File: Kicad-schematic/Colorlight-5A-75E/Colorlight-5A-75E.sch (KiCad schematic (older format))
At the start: 97 parts, among them J1 HUB75 port, J10 HUB75 port, J11 HUB75 port, J12 HUB75 port, J13 HUB75 port, J14 HUB75 port, J15 HUB75 port, J16 HUB75 port, J19 Connector, J2 HUB75 port, J27 JTAG: TCK, J28 SW_Push, J3 HUB75 port, J30 JTAG: TDO, J31 JTAG: TMS, J32 JTAG: TDI, J33 3.3V, J34 GND, J4 HUB75 port, J5 HUB75 port, J6 HUB75 port, J7 HUB75 port, J8 HUB75 port, J9 HUB75 port, U10 74HC245, U11 74HC245, U12 74HC245, U13 74HC245, U14 74HC245, U15 74HC245, U16 74HC245, U17 74HC245, U18 74HC245, U19 74HC245, U20 74HC245, U21 74HC245, U22 74HC245, U23 74HC245, U24 74HC245, U25 74HC245, U26 74HC245, U27 74HC245, U28 74HC245, U29 M12L16161A, U30 74HC245, U31 W25Q32JVSSIQ, U32 M12L16161A, U33 LFE5U-25F-6BG256C, U38 74HC245, U39 74HC245, U9 74HC245

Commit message: Revert "Add nomenclature connections"
This reverts commit 12718895a0fb5e613c60318a09c710380de19625.
Fix issues
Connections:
- net labels added: +3.3V, GND, J1_1, J1_2, J1_3, J1_5, J1_6, J1_7, Jx_B16, Jx_F12, Jx_F15, Jx_J14, Jx_J5, Jx_K1, Jx_K2, Jx_L2, PL2B, PL2C, PT11B, PT15B, PT18A, PT18B, PT22A, PT22B, PT24A, PT24B, PT27A, PT27B, PT29A, PT33A, PT35A, PT38A, PT38B, PT40A, PT40B, PT42A, PT44B, PT47A, PT47B, PT49B, PT4A, PT4B, PT51A, PT53A, PT56A, PT56B, PT60A, PT62A, SPI_CCLK, SPI_CS, SPI_MISO, SPI_MOSI, TCK, TDI, TDO, TMS, U32_A4, U32_A7, U32_A8, U32_A9, U32_B10, U32_B11, U32_B12, U32_B7, U32_B8, U32_C12, U32_C4, U32_C6, U32_C7, U32_C8, U32_D10, U32_D11, U32_D13, U32_D3, U32_D4, U32_D5, U32_D6, U32_D7, U32_D8, U32_D9, U32_E10, U32_E11, U32_E2, U32_E4, U32_E5, U32_E6, U32_E7, U32_E9
- wire segments 256 -> 544
- no-connect marks 0 -> 1
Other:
- moved on the sheet: U29, U33

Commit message: Add nomenclature connections
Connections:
- net labels removed: +3.3V, GND, J1_1, J1_2, J1_3, J1_5, J1_6, J1_7, Jx_B16, Jx_F12, Jx_F15, Jx_J14, Jx_J5, Jx_K1, Jx_K2, Jx_L2, PL2B, PL2C, PT11B, PT15B, PT18A, PT18B, PT22A, PT22B, PT24A, PT24B, PT27A, PT27B, PT29A, PT33A, PT35A, PT38A, PT38B, PT40A, PT40B, PT42A, PT44B, PT47A, PT47B, PT49B, PT4A, PT4B, PT51A, PT53A, PT56A, PT56B, PT60A, PT62A, SPI_CCLK, SPI_CS, SPI_MISO, SPI_MOSI, TCK, TDI, TDO, TMS, U32_A4, U32_A7, U32_A8, U32_A9, U32_B10, U32_B11, U32_B12, U32_B7, U32_B8, U32_C12, U32_C4, U32_C6, U32_C7, U32_C8, U32_D10, U32_D11, U32_D13, U32_D3, U32_D4, U32_D5, U32_D6, U32_D7, U32_D8, U32_D9, U32_E10, U32_E11, U32_E2, U32_E4, U32_E5, U32_E6, U32_E7, U32_E9
- wire segments 544 -> 256
- no-connect marks 1 -> 0
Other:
- moved on the sheet: U29, U33

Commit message: Add Memory Connections
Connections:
- net labels added: +3.3V, GND, PL2B, PL2C, PT11B, PT15B, PT18A, PT18B, PT22A, PT22B, PT24A, PT24B, PT27A, PT27B, PT29A, PT33A, PT35A, PT38A, PT38B, PT40A, PT40B, PT42A, PT44B, PT47A, PT47B, PT49B, PT4A, PT4B, PT51A, PT53A, PT56A, PT56B, PT60A, PT62A, SPI_CCLK, SPI_CS, SPI_MISO, SPI_MOSI, TCK, TDI, TDO, TMS
- wire segments 256 -> 116
- no-connect marks 0 -> 1
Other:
- moved on the sheet: U29, U33

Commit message: Add U32 connection
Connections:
- net +3V3: now also U32.34 (CKE)
- net GND: now also J1.4 (Pin_4), U32.14 (LDQM), U32.18 (~CS), U32.36 (UDQM)
- net PT22A: now also U32.35 (CLK)
- net PT24A: now also U32.16 (~CAS)
- net PT24B: now also U32.17 (~RAS)
- net PT27A: now also U32.15 (~WE)
- net PT27B: now also U32.32 (A9)
- net PT29A: now also U32.19 (BA)
- net PT35A: now also U32.20 (A10/AP)
- net PT40A: now also U32.31 (A8)
- net PT40B: now also U32.30 (A7)
- net PT42A: now also U32.21 (A0)
- net PT47A: now also U32.29 (A6)
- net PT51A: now also U32.28 (A5)
- net PT56A: now also U32.23 (A2)
- net PT56B: now also U32.27 (A4)
- net PT62A: now also U32.24 (A3)
- net U32_A4: now reaches U33.A4 (PT6B)
- net U32_A4: now also U32.8 (DQ4)
- net U32_A8: now reaches U33.A8 (PT29B)
- net U32_A8: now also U32.43 (DQ11)
- net U32_B10: now reaches U33.B10 (PT44A)
- net U32_B10: now also U32.46 (DQ13)
- net U32_B11: now reaches U33.B11 (PT49A)
- net U32_B11: now also U32.48 (DQ14)
- net U32_B8: now reaches U33.B8 (PT35B)
- net U32_B8: now also U32.45 (DQ12)
- net U32_D3: now reaches U33.D3 (PL2D)
- net U32_D3: now also U32.5 (DQ2)
- net U32_D4: now reaches U33.D4 (PT9B)
- net U32_D4: now also U32.9 (DQ5)
- net U32_D5: now reaches U33.D5 (PT13B)
- net U32_D5: now also U32.12 (DQ7)
- net U32_D6: now reaches U33.D6 (PT20B)
- net U32_D6: now also U32.39 (DQ8)
- net U32_D8: now reaches U33.D8 (PT33B)
- net U32_D8: now also U32.42 (DQ10)
- net U32_E2: now reaches U33.E2 (PL8B)
- net U32_E2: now also U32.2 (DQ0)
- net U32_E4: now reaches U33.E4 (PT9A)
- net U32_E4: now also U32.3 (DQ1)
- net U32_E5: now reaches U33.E5 (PT13A)
- net U32_E5: now also U32.6 (DQ3)
- net U32_E6: now reaches U33.E6 (PT20A)
- net U32_E6: now also U32.40 (DQ9)
- net J1_1: now reaches J1.1 (Pin_1)
- net J1_10: now reaches J1.10 (Pin_10)
- net J1_11: now reaches J1.11 (Pin_11)
- net J1_12: now reaches J1.12 (Pin_12)
- net J1_13: now reaches J1.13 (Pin_13)
- net J1_14: now reaches J1.14 (Pin_14)
- net J1_15: now reaches J1.15 (Pin_15)
- net J1_16: now reaches J1.16 (Pin_16)
- net J1_2: now reaches J1.2 (Pin_2)
- net J1_3: now reaches J1.3 (Pin_3)
- net J1_5: now reaches J1.5 (Pin_5)
- net J1_6: now reaches J1.6 (Pin_6)
- net J1_7: now reaches J1.7 (Pin_7)
- net J1_8: now reaches J1.8 (Pin_8)
- net J1_9: now reaches J1.9 (Pin_9)
- net U32_C4: now reaches U32.11 (DQ6)
- net U32_E10: now reaches U32.22 (A1)
- net U32_E11: now reaches U32.49 (DQ15)

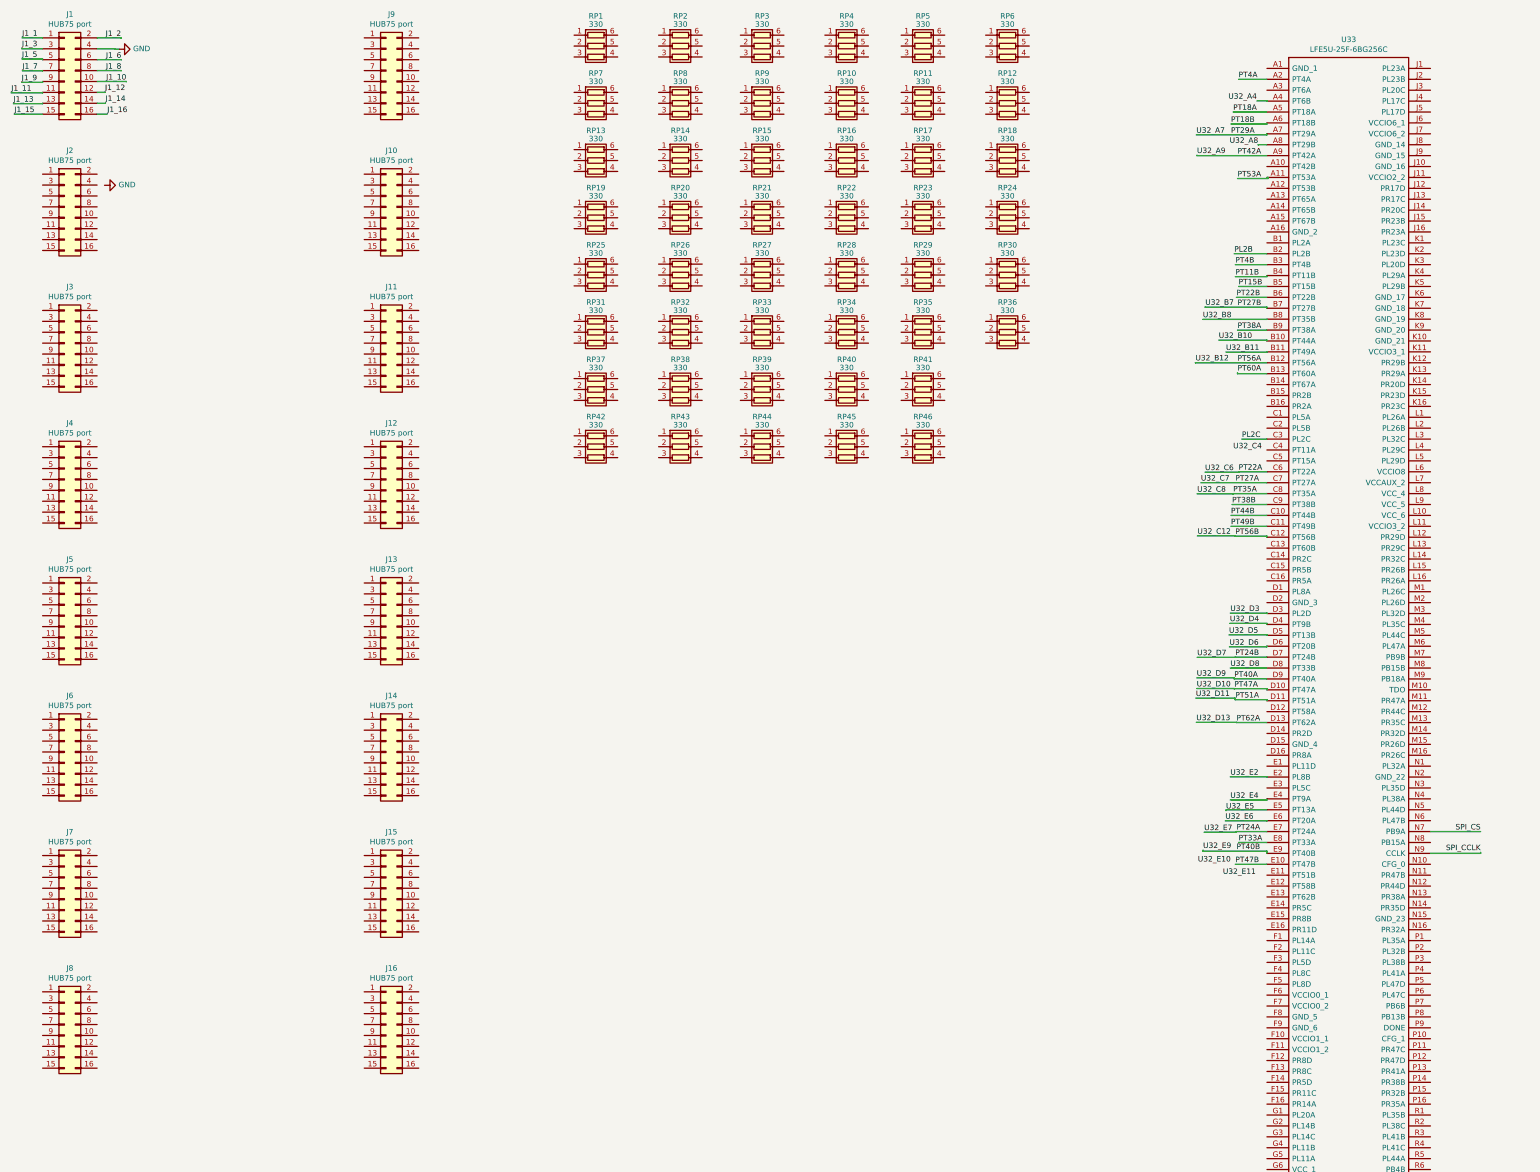
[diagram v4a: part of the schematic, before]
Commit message: Add common Jx Connections
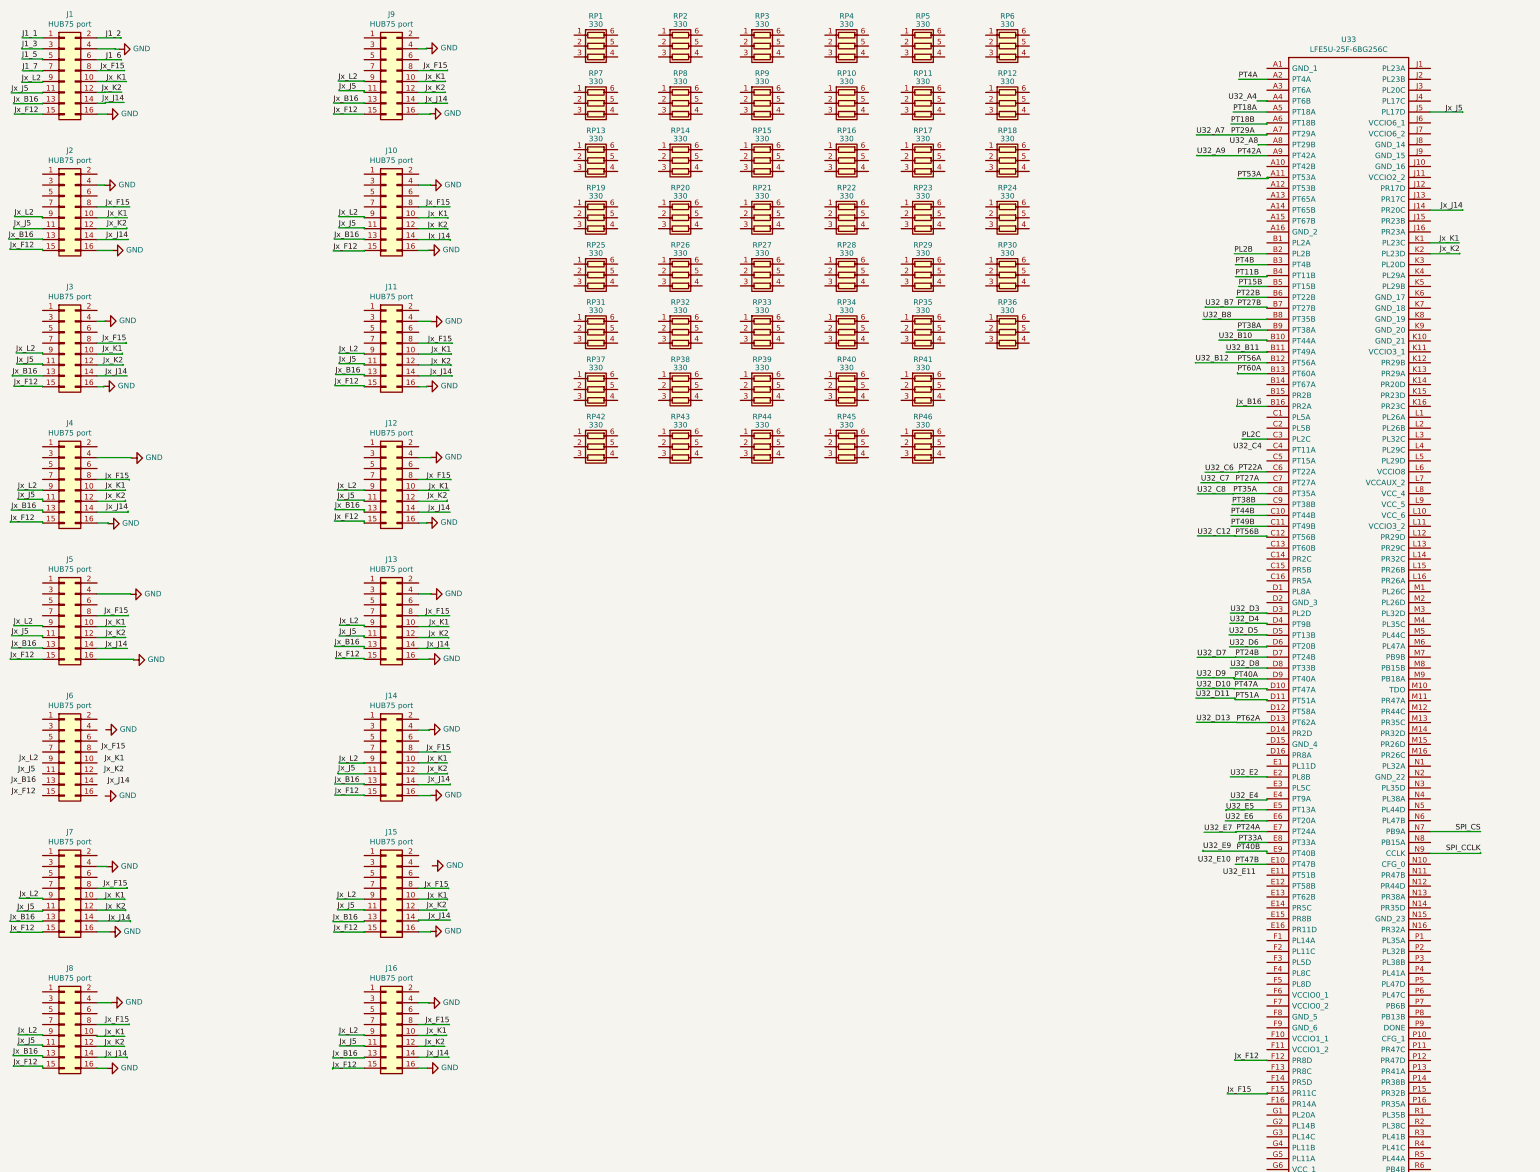
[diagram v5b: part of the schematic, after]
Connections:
- net J1_10 is gone; now on net Jx_K1: J1.10 (Pin_10)
- net J1_11 is gone; now on net Jx_J5: J1.11 (Pin_11)
- net J1_12 is gone; now on net Jx_K2: J1.12 (Pin_12)
- net J1_13 is gone; now on net Jx_B16: J1.13 (Pin_13)
- net J1_14 is gone; now on net Jx_J14: J1.14 (Pin_14)
- net J1_15 is gone; now on net Jx_F12: J1.15 (Pin_15)
- net J1_16 is gone; now on net GND: J1.16 (Pin_16)
- net J1_8 is gone; now on net Jx_F15: J1.8 (Pin_8)
- net J1_9 is gone; now on net Jx_L2: J1.9 (Pin_9)
- net GND: now also J10.16 (Pin_16), J10.4 (Pin_4), J11.16 (Pin_16), J11.4 (Pin_4), J12.16 (Pin_16), J12.4 (Pin_4), J13.16 (Pin_16), J13.4 (Pin_4), J14.16 (Pin_16), J14.4 (Pin_4), J15.16 (Pin_16), J16.16 (Pin_16), J16.4 (Pin_4), J2.16 (Pin_16), J2.4 (Pin_4), J3.16 (Pin_16), J3.4 (Pin_4), J4.16 (Pin_16), J4.4 (Pin_4), J5.16 (Pin_16), J5.4 (Pin_4), J7.16 (Pin_16), J7.4 (Pin_4), J8.16 (Pin_16), J8.4 (Pin_4), J9.16 (Pin_16), J9.4 (Pin_4)
- net Jx_B16: now reaches U33.B16 (PR2A)
- net Jx_B16: now also J10.13 (Pin_13), J11.13 (Pin_13), J12.13 (Pin_13), J13.13 (Pin_13), J14.13 (Pin_13), J15.13 (Pin_13), J16.13 (Pin_13), J2.13 (Pin_13), J3.13 (Pin_13), J4.13 (Pin_13), J5.13 (Pin_13), J7.13 (Pin_13), J8.13 (Pin_13), J9.13 (Pin_13)
- net Jx_F12: now reaches U33.F12 (PR8D)
- net Jx_F12: now also J10.15 (Pin_15), J11.15 (Pin_15), J12.15 (Pin_15), J13.15 (Pin_15), J14.15 (Pin_15), J15.15 (Pin_15), J16.15 (Pin_15), J2.15 (Pin_15), J3.15 (Pin_15), J4.15 (Pin_15), J5.15 (Pin_15), J7.15 (Pin_15), J8.15 (Pin_15), J9.15 (Pin_15)
- net Jx_F15: now reaches U33.F15 (PR11C)
- net Jx_F15: now also J10.8 (Pin_8), J11.8 (Pin_8), J12.8 (Pin_8), J13.8 (Pin_8), J14.8 (Pin_8), J15.8 (Pin_8), J16.8 (Pin_8), J2.8 (Pin_8), J3.8 (Pin_8), J4.8 (Pin_8), J5.8 (Pin_8), J7.8 (Pin_8), J8.8 (Pin_8), J9.8 (Pin_8)
- net Jx_J14: now reaches U33.J14 (PR20C)
- net Jx_J14: now also J10.14 (Pin_14), J11.14 (Pin_14), J12.14 (Pin_14), J13.14 (Pin_14), J14.14 (Pin_14), J15.14 (Pin_14), J16.14 (Pin_14), J2.14 (Pin_14), J3.14 (Pin_14), J4.14 (Pin_14), J5.14 (Pin_14), J7.14 (Pin_14), J8.14 (Pin_14), J9.14 (Pin_14)
- net Jx_J5: now reaches U33.J5 (PL17D)
- net Jx_J5: now also J10.11 (Pin_11), J11.11 (Pin_11), J12.11 (Pin_11), J13.11 (Pin_11), J14.11 (Pin_11), J15.11 (Pin_11), J16.11 (Pin_11), J2.11 (Pin_11), J3.11 (Pin_11), J4.11 (Pin_11), J5.11 (Pin_11), J7.11 (Pin_11), J8.11 (Pin_11), J9.11 (Pin_11)
- net Jx_K1: now reaches U33.K1 (PL23C)
- net Jx_K1: now also J10.10 (Pin_10), J11.10 (Pin_10), J12.10 (Pin_10), J13.10 (Pin_10), J14.10 (Pin_10), J15.10 (Pin_10), J16.10 (Pin_10), J2.10 (Pin_10), J3.10 (Pin_10), J4.10 (Pin_10), J5.10 (Pin_10), J7.10 (Pin_10), J8.10 (Pin_10), J9.10 (Pin_10)
- net Jx_K2: now reaches U33.K2 (PL23D)
- net Jx_K2: now also J10.12 (Pin_12), J11.12 (Pin_12), J12.12 (Pin_12), J13.12 (Pin_12), J14.12 (Pin_12), J15.12 (Pin_12), J16.12 (Pin_12), J2.12 (Pin_12), J3.12 (Pin_12), J4.12 (Pin_12), J5.12 (Pin_12), J7.12 (Pin_12), J8.12 (Pin_12), J9.12 (Pin_12)
- net Jx_L2: now reaches J2.9 (Pin_9)
- net Jx_L2: now also J10.9 (Pin_9), J11.9 (Pin_9), J12.9 (Pin_9), J13.9 (Pin_9), J14.9 (Pin_9), J15.9 (Pin_9), J16.9 (Pin_9), J3.9 (Pin_9), J4.9 (Pin_9), J5.9 (Pin_9), J7.9 (Pin_9), J8.9 (Pin_9), J9.9 (Pin_9)

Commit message: Add J1,J2, J3  connections
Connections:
- net J1_1 is gone; now on net J1_F3: J1.1 (Pin_1)
- net J1_2 is gone; now on net J1_F1: J1.2 (Pin_2)
- net J1_3 is gone; now on net J1_G3: J1.3 (Pin_3)
- net J1_5 is gone; now on net J1_G2: J1.5 (Pin_5)
- net J1_6 is gone; now on net J1_H3: J1.6 (Pin_6)
- net J1_7 is gone; now on net J1_H5: J1.7 (Pin_7)
- net J1_R_G3: now reaches RP1.1 (R1.1)
- net J1_R_G3: now also U28.16 (B2)
- net J1_R_G2: now reaches RP1.2 (R2.1)
- net J1_R_G2: now also U28.15 (B3)
- net J1_R_F1: now reaches RP1.3 (R3.1)
- net J1_R_F1: now also U28.17 (B1)
- net J1_F1: now reaches RP1.4 (R3.2)
- net J1_G2: now reaches RP1.5 (R2.2)
- net J1_G3: now reaches RP1.6 (R1.2)
- net J1_R_F3: now reaches RP7.1 (R1.1)
- net J1_R_F3: now also U28.18 (B0)
- net J1_R_H3: now reaches RP7.2 (R2.1)
- net J1_R_H3: now also U28.14 (B4)
- net J1_R_H5: now reaches RP7.3 (R3.1)
- net J1_R_H5: now also U28.13 (B5)
- net J1_H5: now reaches RP7.4 (R3.2)
- net J1_H3: now reaches RP7.5 (R2.2)
- net J1_F3: now reaches RP7.6 (R1.2)
- net J2_R_G4: now reaches RP13.1 (R1.1)
- net J2_R_G4: now also U10.18 (B0)
- net J2_R_G5: now reaches RP13.2 (R2.1)
- net J2_R_G5: now also U10.17 (B1)
- net J2_R_J2: now reaches RP13.3 (R3.1)
- net J2_R_J2: now also U10.16 (B2)
- net J2_J2: now reaches RP13.4 (R3.2)
- net J2_J2: now also J2.3 (Pin_3)
- net J2_G5: now reaches RP13.5 (R2.2)
- net J2_G5: now also J2.2 (Pin_2)
- net J2_G4: now reaches RP13.6 (R1.2)
- net J2_G4: now also J2.1 (Pin_1)
- net J2_R_H2: now reaches RP19.1 (R1.1)
- net J2_R_H2: now also U10.15 (B3)
- net J2_R_J1: now reaches RP19.2 (R2.1)
- net J2_R_J1: now also U10.14 (B4)
- net J2_R_J3: now reaches RP19.3 (R3.1)
- net J2_R_J3: now also U10.13 (B5)
- net J2_J3: now reaches RP19.4 (R3.2)
- net J2_J3: now also J2.7 (Pin_7)
- net J2_J1: now reaches RP19.5 (R2.2)
- net J2_J1: now also J2.6 (Pin_6)
- net J2_H2: now reaches RP19.6 (R1.2)
- net J2_H2: now also J2.5 (Pin_5)
- net J3_R_J4: now reaches RP25.1 (R1.1)
- net J3_R_J4: now also U13.18 (B0)
- net J3_R_K3: now reaches RP25.2 (R2.1)
- net J3_R_K3: now also U13.17 (B1)
- net J3_R_G1: now reaches RP25.3 (R3.1)
- net J3_R_G1: now also U13.16 (B2)
- net J3_G1: now reaches RP25.4 (R3.2)
- net J3_G1: now also J3.3 (Pin_3)
- net J3_K3: now reaches RP25.5 (R2.2)
- net J3_K3: now also J3.2 (Pin_2)
- net J3_J4: now reaches RP25.6 (R1.2)
- net J3_J4: now also J3.1 (Pin_1)
- net J3_R_K4: now reaches RP31.1 (R1.1)
- net J3_R_K4: now also U13.15 (B3)
- net J3_R_C2: now reaches RP31.2 (R2.1)
- net J3_R_C2: now also U13.14 (B4)
- net J3_R_E3: now reaches RP31.3 (R3.1)
- net J3_R_E3: now also U13.13 (B5)
- net J3_E3: now reaches RP31.4 (R3.2)
- net J3_E3: now also J3.7 (Pin_7)
- net J3_C2: now reaches RP31.5 (R2.2)
- net J3_C2: now also J3.6 (Pin_6)
- net J3_K4: now reaches RP31.6 (R1.2)
- net J3_K4: now also J3.5 (Pin_5)
- net G3: now reaches U28.4 (A2)
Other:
- note added: "J1\n"
- note added: "J2\n"
- note added: "J3\n"
- note added: "J5\n"
- moved on the sheet: RP10, RP11, RP12, RP14, RP15, RP16, RP17, RP18, RP2, RP20, RP21, RP22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

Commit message: more Jx Connections
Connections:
- net GND: now also J6.16 (Pin_16), J6.4 (Pin_4)
- net Jx_B16: now also J6.13 (Pin_13)
- net Jx_F12: now also J6.15 (Pin_15)
- net Jx_F15: now also J6.8 (Pin_8)
- net Jx_J14: now also J6.14 (Pin_14)
- net Jx_J5: now also J6.11 (Pin_11)
- net Jx_K1: now also J6.10 (Pin_10)
- net Jx_K2: now also J6.12 (Pin_12)
- net Jx_L2: now also J6.9 (Pin_9)
- net J4_R_C1: now reaches RP37.1 (R1.1)
- net J4_R_C1: now also U11.18 (B0)
- net J4_R_A3: now reaches RP37.2 (R2.1)
- net J4_R_A3: now also U11.17 (B1)
- net J4_R_F4: now reaches RP37.3 (R3.1)
- net J4_R_F4: now also U11.16 (B2)
- net J4_F4: now reaches RP37.4 (R3.2)
- net J4_F4: now also J4.3 (Pin_3)
- net J4_A3: now reaches RP37.5 (R2.2)
- net J4_A3: now also J4.2 (Pin_2)
- net J4_C1: now reaches RP37.6 (R1.2)
- net J4_C1: now also J4.1 (Pin_1)
- net J4_R_E1: now reaches RP42.1 (R1.1)
- net J4_R_E1: now also U11.15 (B3)
- net J4_R_F5: now reaches RP42.2 (R2.1)
- net J4_R_F5: now also U11.14 (B4)
- net J4_R_D1: now reaches RP42.3 (R3.1)
- net J4_R_D1: now also U11.13 (B5)
- net J4_D1: now reaches RP42.4 (R3.2)
- net J4_D1: now also J4.7 (Pin_7)
- net J4_F5: now reaches RP42.5 (R2.2)
- net J4_F5: now also J4.6 (Pin_6)
- net J4_E1: now reaches RP42.6 (R1.2)
- net J4_E1: now also J4.5 (Pin_5)
- net J5_R_F2: now reaches RP2.1 (R1.1)
- net J5_R_F2: now also U27.13 (B5)
- net J5_R_L5: now reaches RP2.2 (R2.1)
- net J5_R_L5: now also U27.14 (B4)
- net J5_R_R1: now reaches RP2.3 (R3.1)
- net J5_R_R1: now also U27.15 (B3)
- net J5_R1: now reaches RP2.4 (R3.2)
- net J5_R1: now also J5.5 (Pin_5)
- net J5_L5: now reaches RP2.5 (R2.2)
- net J5_L5: now also J5.6 (Pin_6)
- net J5_F2: now reaches RP2.6 (R1.2)
- net J5_F2: now also J5.7 (Pin_7)
- net J6_R_N3: now reaches RP8.1 (R1.1)
- net J6_R_N3: now also U26.18 (B0)
- net J6_R_M4: now reaches RP8.2 (R2.1)
- net J6_R_M4: now also U26.17 (B1)
- net J6_R_T4: now reaches RP8.3 (R3.1)
- net J6_R_T4: now also U26.16 (B2)
- net J6_T4: now reaches RP8.4 (R3.2)
- net J6_T4: now also J6.3 (Pin_3)
- net J6_M4: now reaches RP8.5 (R2.2)
- net J6_M4: now also J6.2 (Pin_2)
- net J6_N3: now reaches RP8.6 (R1.2)
- net J6_N3: now also J6.1 (Pin_1)
- net J6_R_R5: now reaches RP14.1 (R1.1)
- net J6_R_R5: now also U26.15 (B3)
- net J6_R_R3: now reaches RP14.2 (R2.1)
- net J6_R_R3: now also U26.14 (B4)
- net J6_R_N4: now reaches RP14.3 (R3.1)
- net J6_R_N4: now also U26.13 (B5)
- net J6_N4: now reaches RP14.4 (R3.2)
- net J6_N4: now also J6.7 (Pin_7)
- net J6_R3: now reaches RP14.5 (R2.2)
- net J6_R3: now also J6.6 (Pin_6)
- net J6_R5: now reaches RP14.6 (R1.2)
- net J6_R5: now also J6.5 (Pin_5)
- net J9_R_M11: now reaches RP20.1 (R1.1)
- net J9_R_M11: now also U18.18 (B0)
- net J9_R_N11: now reaches RP20.2 (R2.1)
- net J9_R_N11: now also U18.17 (B1)
- net J9_R_P12: now reaches RP20.3 (R3.1)
- net J9_R_P12: now also U18.16 (B2)
- net J9_P12: now reaches RP20.4 (R3.2)
- net J9_P12: now also J9.3 (Pin_3)
- net J9_N11: now reaches RP20.5 (R2.2)
- net J9_N11: now also J9.2 (Pin_2)
- net J9_M11: now reaches RP20.6 (R1.2)
- net J9_M11: now also J9.1 (Pin_1)
- net J9_R_K15: now reaches RP26.1 (R1.1)
- net J9_R_K15: now also U18.15 (B3)
- net J9_R_N12: now reaches RP26.2 (R2.1)
- net J9_R_N12: now also U18.14 (B4)
- net J9_R_L16: now reaches RP26.3 (R3.1)
- net J9_R_L16: now also U18.13 (B5)
- net J9_L16: now reaches RP26.4 (R3.2)
- net J9_L16: now also J9.7 (Pin_7)
- net J9_N12: now reaches RP26.5 (R2.2)
- net J9_N12: now also J9.6 (Pin_6)
- net J9_K15: now reaches RP26.6 (R1.2)
- net J9_K15: now also J9.5 (Pin_5)
- net J5_H4: now reaches J5.1 (Pin_1)
- net J5_H4: now also RP6.6 (R1.2)
- net J5_K5: now reaches J5.2 (Pin_2)
- net J5_K5: now also RP6.5 (R2.2)
- net J5_P1: now reaches J5.3 (Pin_3)
- net J5_P1: now also RP6.4 (R3.2)
- net J5_R_H4: now reaches RP6.1 (R1.1)
- net J5_R_H4: now also U27.18 (B0)
- net J5_R_K5: now reaches RP6.2 (R2.1)
- net J5_R_K5: now also U27.17 (B1)
- net J5_R_P1: now reaches RP6.3 (R3.1)
- net J5_R_P1: now also U27.16 (B2)
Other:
- moved on the sheet: J4, J5, RP10, RP11, RP12, RP14, RP15, RP16, RP17, RP18, RP2, RP20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
